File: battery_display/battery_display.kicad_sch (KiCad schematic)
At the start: 20 parts, among them J1 FH34SRJ-24S-0.5SH_99_, Q1 ZXM61N03F, Q2 ZXM61N03F, SW1 Button-THT - 2-1825910-7

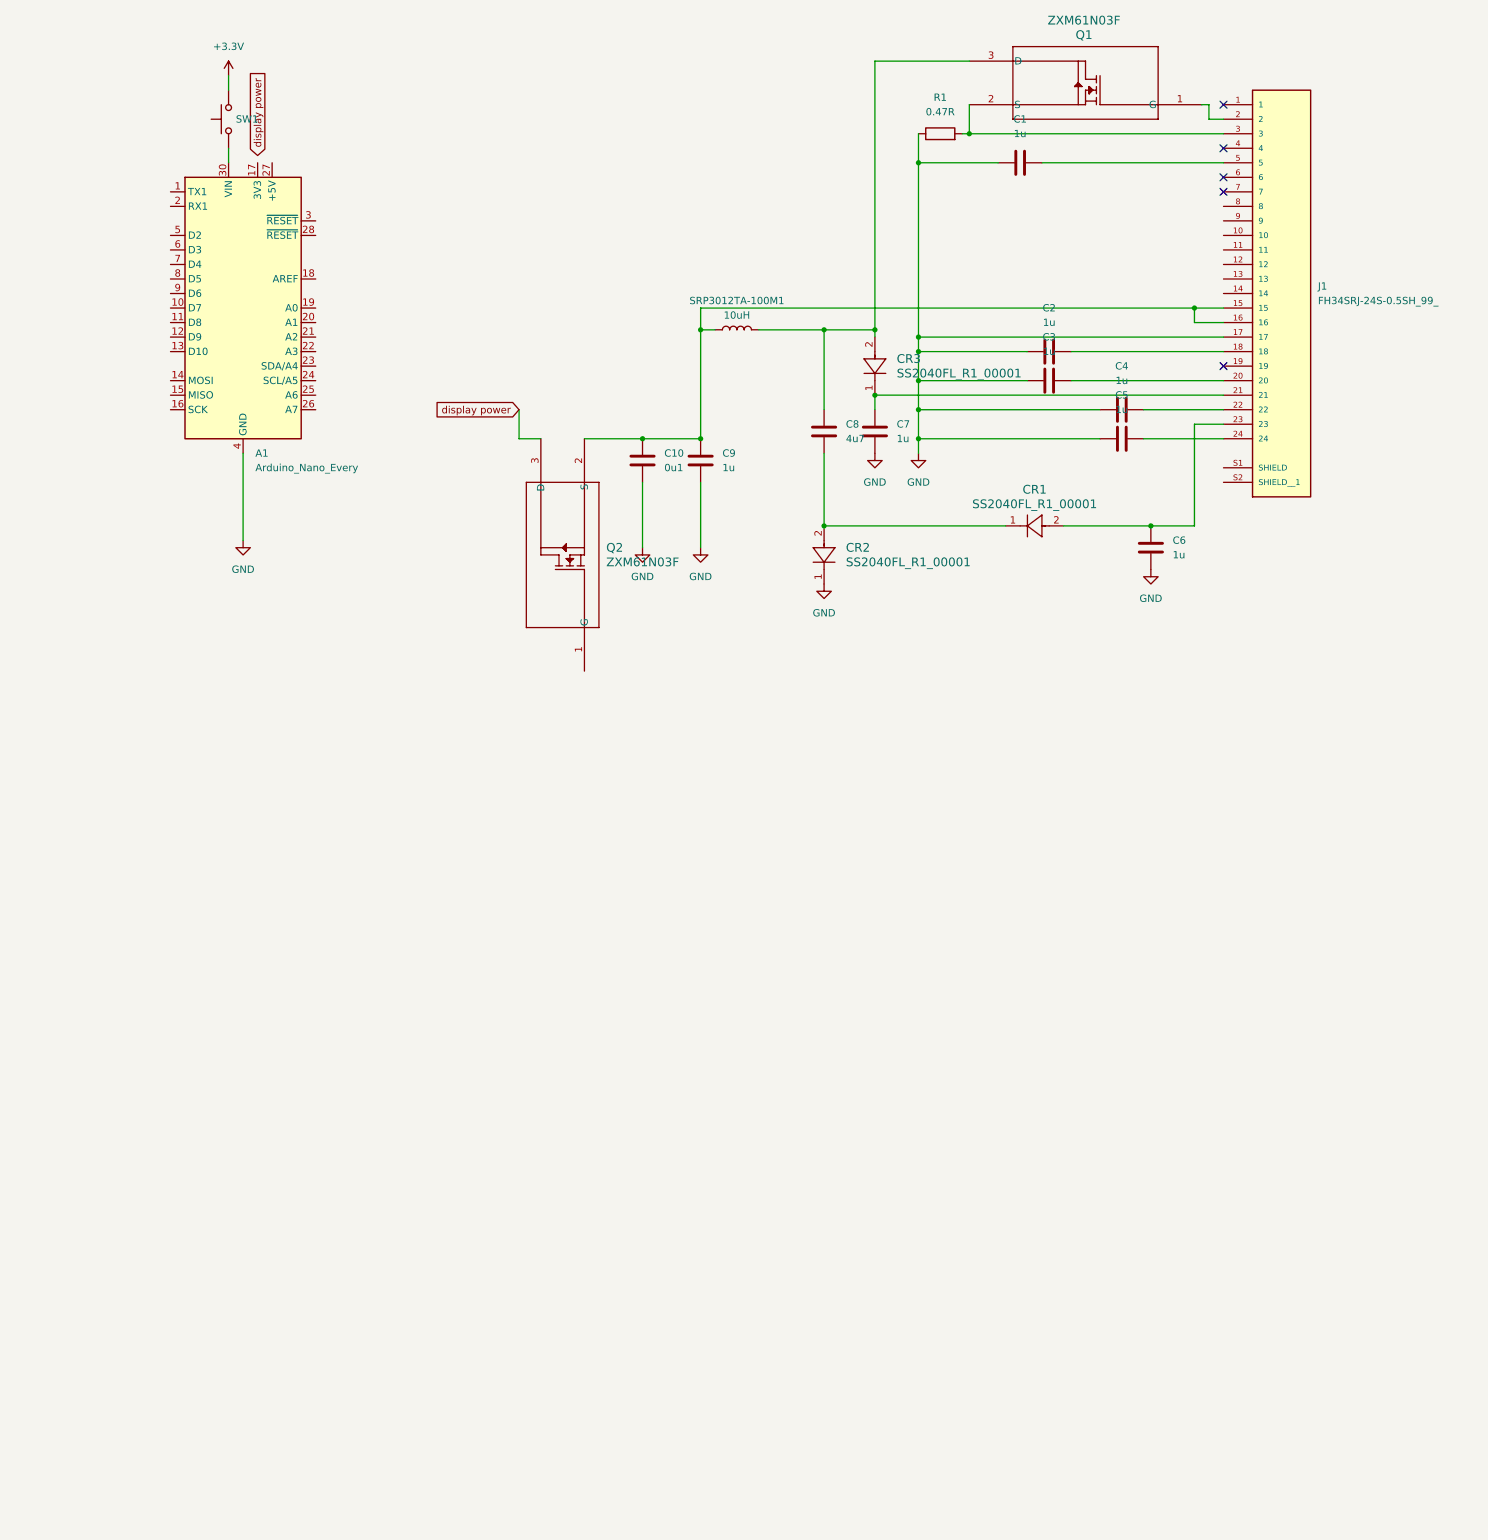
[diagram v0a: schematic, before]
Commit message: Completed PCB Layout
- also added voltage divider for reading voltage of the battery
- next step ask coco for conformation
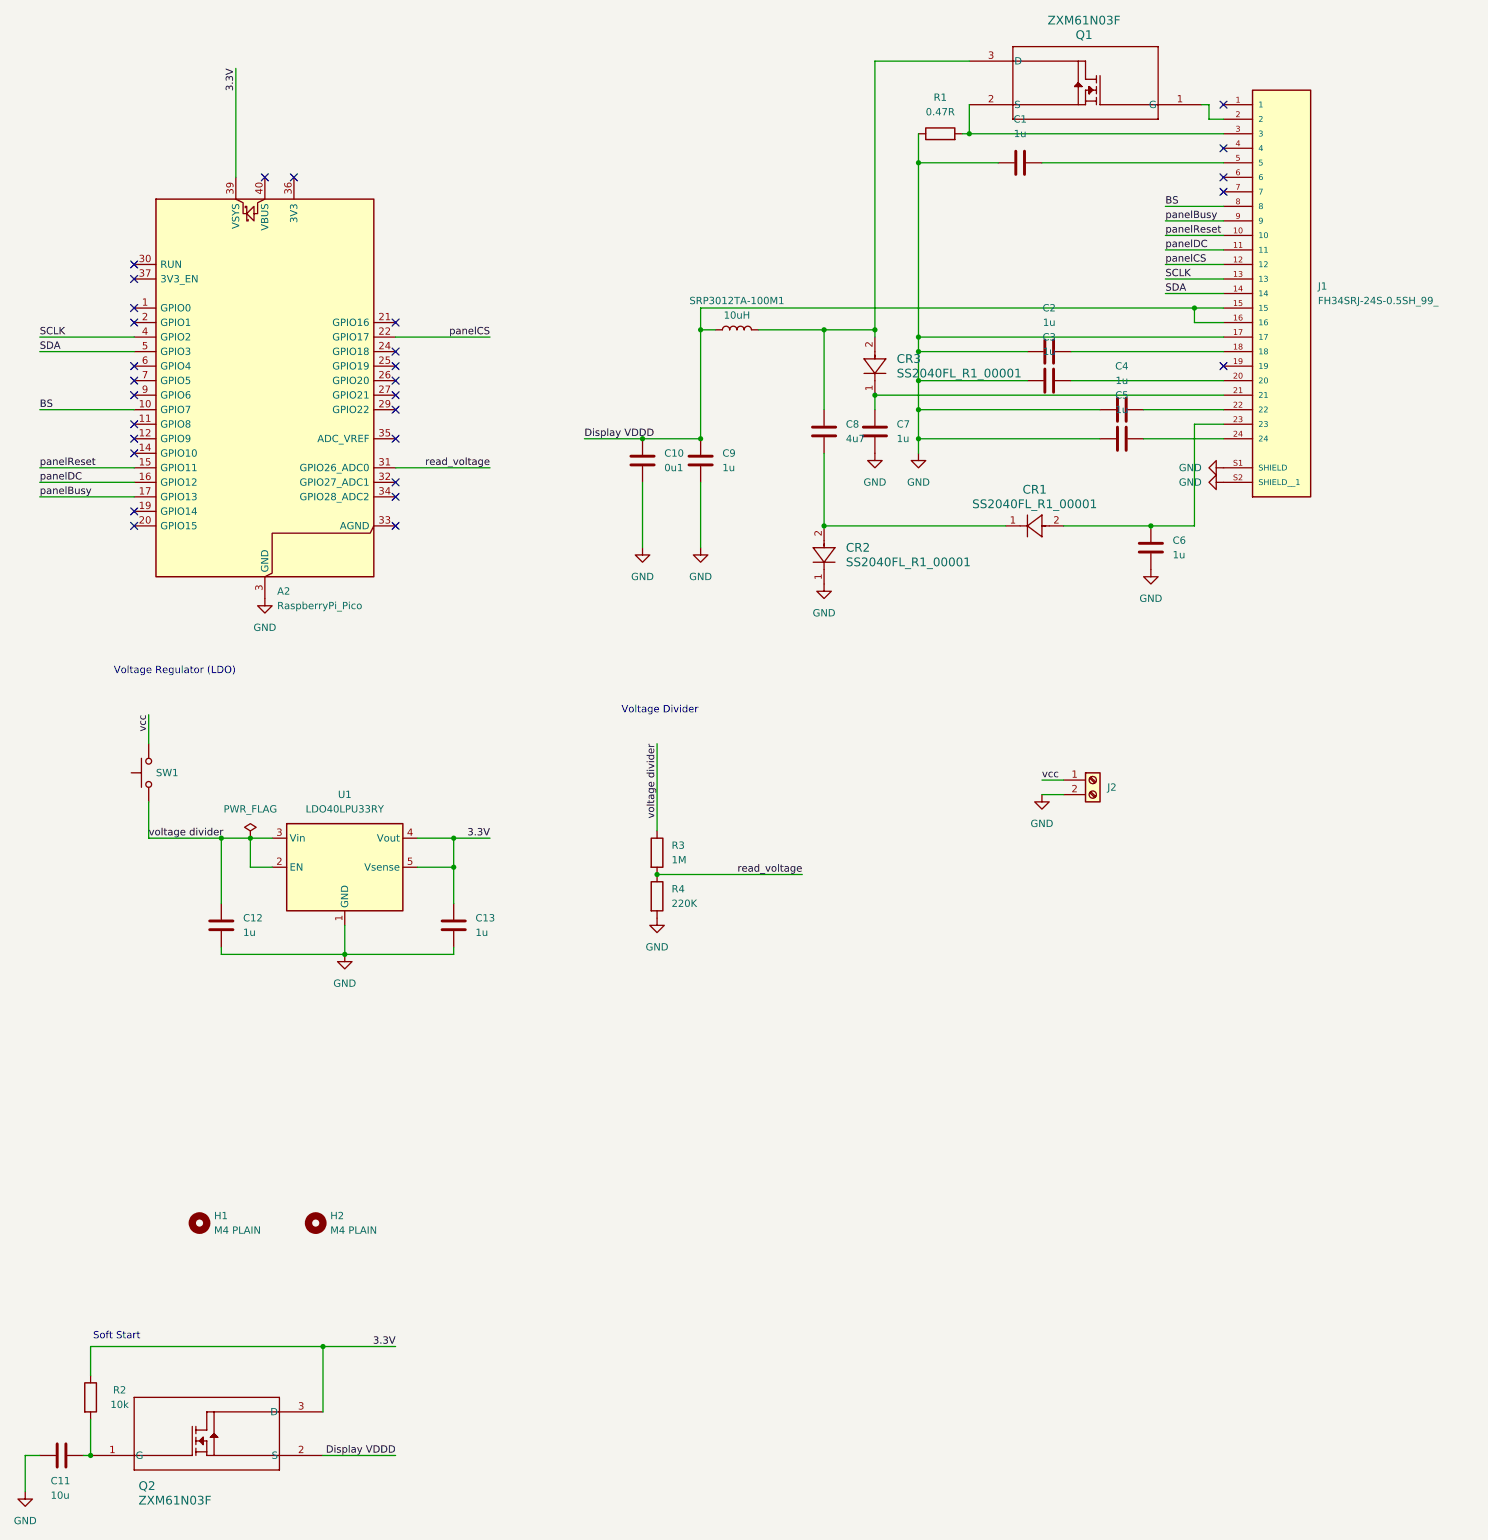
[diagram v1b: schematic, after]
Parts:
- removed A1: Arduino_Nano_Every, Module:Arduino_Nano, symbol MCU_Module:Arduino_Nano_Every
- added A2: RaspberryPi_Pico, Module:RaspberryPi_Pico_Common_Unspecified, symbol MCU_Module:RaspberryPi_Pico
- added C11: 10u, rsx_capacitors:C_0805_2012Metric, symbol rsx_Capacitors:10u
- added C12, C13: 1u, rsx_capacitors:C_0805_2012Metric, symbol rsx_Capacitors:1u
- added H1, H2: M4 PLAIN, rsx_misc:MountingHole_4.5mm, symbol rsx_misc:M4 PLAIN
- added J2: Screw_Terminal_2x2.54, rsx_headers_screw:Wurth_691210910002, symbol rsx_header_screw:Screw_Terminal_2x2.54
- added R2: 10k, rsx_resistors:R_0603_1608Metric, symbol rsx_Resistors:10k
- added R3: 1M, rsx_resistors:R_0603_1608Metric, symbol rsx_Resistors:1M
- added R4: 220K, rsx_resistors:R_0603_1608Metric, symbol rsx_Resistors:220K
- added U1: LDO40LPU33RY, Package_DFN_QFN:DFN-6-1EP_3x3mm_P0.95mm_EP1.7x2.6mm, symbol Regulator_Linear:LDO40LPU33RY
- J1: DPN (none) -> H124725CT-ND; MPN (none) -> FH34SRJ-24S-0.5SH(99)
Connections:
- net GND: now also J1.S1 (SHIELD), J1.S2 (SHIELD__1), A2.13 (GND), A2.18 (GND), A2.23 (GND), A2.28 (GND), A2.3 (GND), A2.38 (GND), A2.8 (GND), C11.2, C12.2, C13.2, J2.2 (Pin_2), R4.2, U1.1 (GND), U1.7 (GND)
- net panelReset: now reaches J1.10
- net panelReset: now also A2.15 (GPIO11)
- net panelDC: now reaches J1.11
- net panelDC: now also A2.16 (GPIO12)
- net panelCS: now reaches J1.12
- net panelCS: now also A2.22 (GPIO17)
- net SCLK: now reaches J1.13
- net SCLK: now also A2.4 (GPIO2)
- net SDA: now reaches J1.14
- net SDA: now also A2.5 (GPIO3)
- net Display VDDD: now reaches C10.1, C9.1, J1.15, J1.16, Q2.2 (S), SRP3012TA-100M1.1
- net BS: now reaches J1.8
- net BS: now also A2.10 (GPIO7)
- net panelBusy: now reaches J1.9
- net panelBusy: now also A2.17 (GPIO13)
- net voltage divider: now reaches SW1.1
- net voltage divider: now also C12.1, R3.1, U1.2 (EN), U1.3 (Vin)
- net at Q2.1 (G): now also C11.1, R2.2
- net +3.3V renamed vcc
- net vcc: now also J2.1 (Pin_1)
- net display power renamed 3.3V
- net 3.3V: now also A2.39 (VSYS), C13.1, R2.1, U1.4 (Vout), U1.5 (Vsense)
- new net read_voltage: A2.31 (GPIO26_ADC0), R3.2, R4.1
- no-connect marks 5 -> 29
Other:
- note added: "Soft Start"
- note added: "Voltage Divider"
- note added: "Voltage Regulator (LDO)"
- moved on the sheet: Q2, SW1

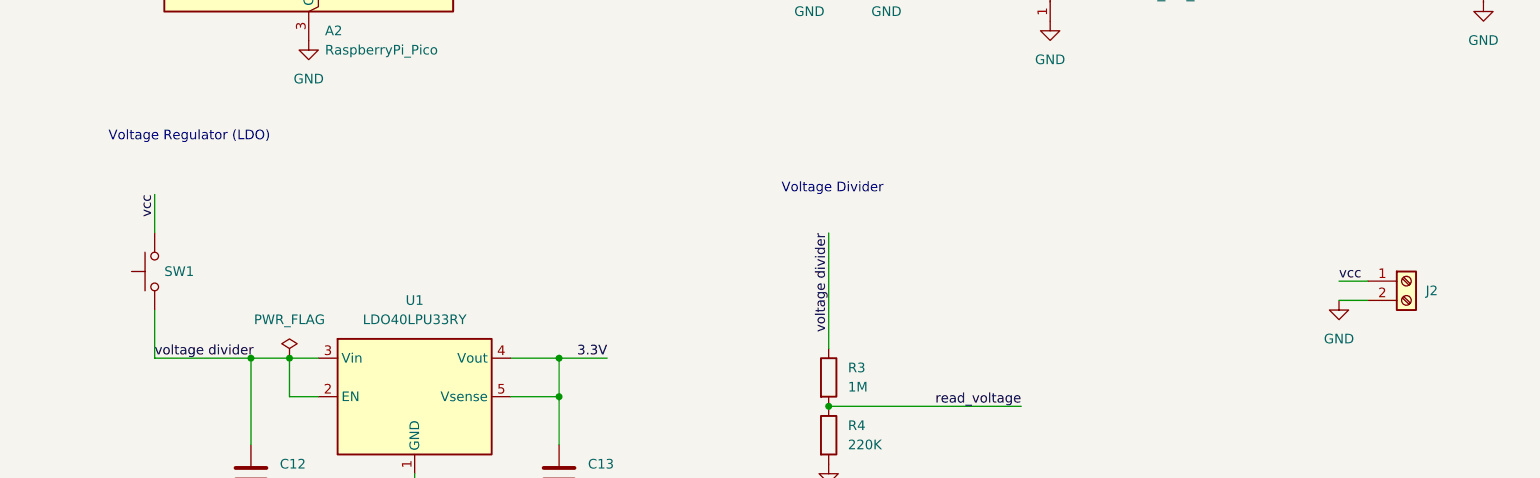
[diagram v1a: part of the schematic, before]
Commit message: Reapply "Added some small fixes"
This reverts commit d414565db0f35087673e5f9750bdaf74336bf2be.
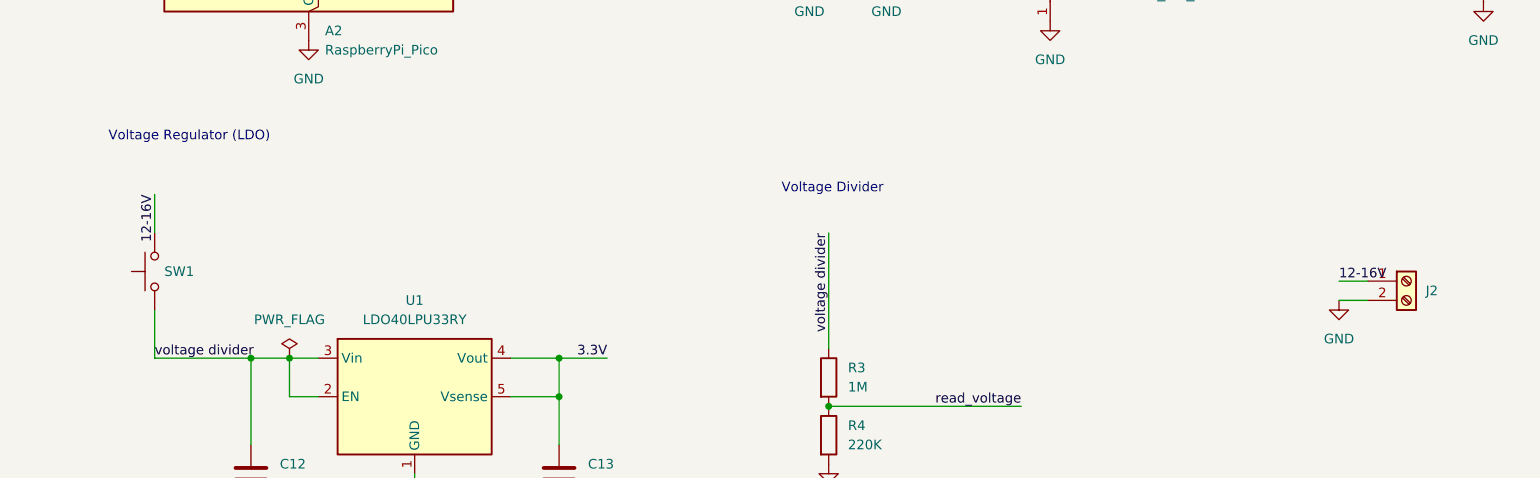
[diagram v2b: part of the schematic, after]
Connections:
- net vcc renamed 12-16V
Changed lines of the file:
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@@
 		)
 	)
-	(label "vcc"
+	(label "12-16V"
 		(at 39.37 139.7 270)
 		(effects
@@
 		)
 	)
-	(label "vcc"
+	(label "12-16V"
 		(at 195.58 151.13 0)
 		(effects

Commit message: Moved the display connector closer to the RPi
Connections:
- net SCLK: now also A2.27 (GPIO21); no longer A2.4 (GPIO2)
- net SDA: now also A2.26 (GPIO20); no longer A2.5 (GPIO3)
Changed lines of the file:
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@@
+	)
+	(no_connect
+		(at 36.83 76.2)
 	)
 	(no_connect
@@
 	)
 	(no_connect
-		(at 82.55 81.28)
+		(at 36.83 73.66)
 	)
 	(no_connect
@@
 	)
 	(no_connect
-		(at 82.55 83.82)
-	)
-	(no_connect
 		(at 64.77 45.72)
 	)
@@
 	(wire
 		(pts
+			(xy 82.55 83.82) (xy 99.06 83.82)
+		)
+		(stroke
+			(width 0)
+			(type default)
+		)
+	)
+	(wire
+		(pts
 			(xy 29.21 255.27) (xy 29.21 250.19)
 		)
@@
 	(wire
 		(pts
-			(xy 20.32 76.2) (xy 36.83 76.2)
-		)
-		(stroke
-			(width 0)
-			(type default)
-		)
-	)
-	(wire
-		(pts
-			(xy 20.32 73.66) (xy 36.83 73.66)
-		)
-		(stroke
-			(width 0)
-			(type default)
-		)
-	)
-	(wire
-		(pts
 			(xy 173.99 86.36) (xy 205.74 86.36)
 		)
@@
 		(pts
 			(xy 17.78 269.24) (xy 17.78 275.59)
+		)
+		(stroke
+			(width 0)
+			(type default)
+		)
+	)
+	(wire
+		(pts
+			(xy 82.55 81.28) (xy 99.06 81.28)
 		)
 		(stroke
@@
 		)
 	)
+	(label "SCLK"
+		(at 99.06 83.82 180)
+		(effects
+			(font
+				(size 1.27 1.27)
+			)
+			(justify right bottom)
+		)
+	)
 	(label "panelDC"
 		(at 20.32 99.06 0)
@@
 	)
 	(label "SDA"
-		(at 20.32 76.2 0)
-		(effects
-			(font
-				(size 1.27 1.27)
-			)
-			(justify left bottom)
-		)
-	)
-	(label "SDA"
 		(at 217.17 66.04 0)
 		(effects
@@
 		)
 	)
+	(label "SDA"
+		(at 99.06 81.28 180)
+		(effects
+			(font
+				(size 1.27 1.27)
+			)
+			(justify right bottom)
+		)
+	)
 	(label "read_voltage"
 		(at 99.06 96.52 180)
@@
 		(effects
 			(font
-				(size 1.27 1.27)
-			)
-			(justify left bottom)
-		)
-	)
-	(label "SCLK"
-		(at 20.32 73.66 0)
-		(effects
-			(font

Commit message: fixed traumatic errors
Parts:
- removed C10: 0u1, Capacitor_SMD:C_01005_0402Metric, symbol rsx_Capacitors:0u1_0402
- added C14: 100n, CAPC17595_95N_KEM, symbol rsx_Capacitors:100n
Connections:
- net Display VDDD: now also C14.2
- net GND: now also C14.1
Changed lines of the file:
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@@
 	)
 	(junction
+		(at 125.73 91.44)
+		(diameter 0)
+		(color 0 0 0 0)
+	)
+	(junction
 		(at 69.85 250.19)
 		(diameter 0)
@@
 	)
 	(junction
-		(at 125.73 91.44)
-		(diameter 0)
-		(color 0 0 0 0)
-	)
-	(junction
 		(at 173.99 73.66)
 		(diameter 0)
@@
 	(wire
 		(pts
-			(xy 125.73 91.44) (xy 135.89 91.44)
+			(xy 115.57 91.44) (xy 125.73 91.44)
 		)
 		(stroke
@@
 	(wire
 		(pts
-			(xy 173.99 76.2) (xy 193.04 76.2)
+			(xy 125.73 91.44) (xy 135.89 91.44)
 		)
 		(stroke
@@
 	(wire
 		(pts
-			(xy 115.57 91.44) (xy 125.73 91.44)
+			(xy 173.99 76.2) (xy 193.04 76.2)
 		)
 		(stroke
@@
 	)
 	(symbol
-		(lib_id "rsx_Capacitors:0u1_0402")
-		(at 125.73 95.25 0)
-		(unit 1)
-		(exclude_from_sim no)
-		(in_bom yes)
-		(on_board yes)
-		(dnp no)
-		(fields_autoplaced yes)
-		(property "Reference" "C10"
-			(at 129.54 93.9799 0)
-			(effects
-				(font
-					(size 1.27 1.27)
-				)
-				(justify left)
-			)
-		)
-		(property "Value" "0u1"
-			(at 129.54 96.5199 0)
-			(effects
-				(font
-					(size 1.27 1.27)
-				)
-				(justify left)
-			)
-		)
-		(property "Footprint" "Capacitor_SMD:C_01005_0402Metric"
-			(at 126.6952 99.06 0)
-			(effects
-				(font
-					(size 1.27 1.27)
-				)
-				(hide yes)
-			)
-		)
-		(property "Datasheet" "https://mm.digikey.com/Volume0/opasdata/d220001/medias/docus/503/CL05A104KA5NNNC.pdf"
-			(at 125.73 95.25 0)
-			(effects
-				(font
-					(size 1.27 1.27)
-				)
-				(hide yes)
-			)
-		)
-		(property "Description" "CAP CER 0.1UF 25V X5R 0402"
-			(at 125.73 95.25 0)
-			(effects
-				(font
-					(size 1.27 1.27)
-				)
-				(hide yes)
-			)
-		)
-		(property "MFR" "Samsung Electro-Mechanics"
-			(at 125.73 95.25 0)
-			(effects
-				(font
-					(size 1.27 1.27)
-				)
-				(hide yes)
-			)
-		)
-		(property "DPN" "1276-1043-1-ND"
-			(at 125.73 95.25 0)
-			(effects
-				(font
-					(size 1.27 1.27)
-				)
-				(hide yes)
-			)
-		)
-		(property "MPN" "CL05A104KA5NNNC"
-			(at 125.73 95.25 0)
-			(effects
-				(font
-					(size 1.27 1.27)
-				)
-				(hide yes)
-			)
-		)
-		(pin "1"
-		)
-		(pin "2"
-		)
-		(instances
-			(project ""
-				(path "/9c37534e-0246-46b3-81ad-6273e0189fcc"
-					(reference "C10")
-					(unit 1)
-				)
-			)
-		)
-	)
-	(symbol
 		(lib_id "power:GND")
 		(at 227.33 96.52 270)
@@
 					(unit 1)
 				)
+			)
+		)
+	)
+	(symbol
+		(lib_id "rsx_Capacitors:100n")
+		(at 125.73 99.06 90)
+		(unit 1)
+		(exclude_from_sim no)
+		(in_bom yes)
+		(on_board yes)
+		(dnp no)
+		(fields_autoplaced yes)
+		(property "Reference" "C14"
+			(at 129.54 93.9799 90)
+			(effects
+				(font
+					(size 1.524 1.524)
+				)
+				(justify right)
+			)
+		)
+		(property "Value" "100n"
+			(at 129.54 96.5199 90)
+			(effects
+				(font
+					(size 1.524 1.524)
+				)
+				(justify right)
+			)
+		)
+		(property "Footprint" "CAPC17595_95N_KEM"
+			(at 125.73 99.06 0)
+			(effects
+				(font
+					(size 1.27 1.27)
+					(italic yes)
+				)
+				(hide yes)
+			)
+		)
+		(property "Datasheet" "https://content.kemet.com/datasheets/KEM_C1002_X7R_SMD.pdf"
+			(at 125.73 99.06 0)
+			(effects
+				(font
+					(size 1.27 1.27)
+					(italic yes)
+				)
+				(hide yes)
+			)
+		)
+		(property "Description" "0.1 µF ±10% 50V Ceramic Capacitor X7R 0603 (1608 Metric)"
+			(at 125.73 99.06 0)
+			(effects
+				(font
+					(size 1.27 1.27)
+				)
+				(hide yes)
+			)
+		)
+		(property "DPN" "399-C0603C104K5RACTUCT-ND"
+			(at 125.73 99.06 0)
+			(effects
+				(font
+					(size 1.27 1.27)
+				)
+				(hide yes)
+			)
+		)
+		(property "MPN" "C0603C104K5RACTU"
+			(at 125.73 99.06 0)
+			(effects
+				(font
+					(size 1.27 1.27)
+				)
+				(hide yes)
+			)
+		)
+		(pin "2"
+		)
+		(pin "1"
+		)
+		(instances
+			(project ""
+				(path "/9c37534e-0246-46b3-81ad-6273e0189fcc"
+					(reference "C14")
+					(unit 1)
+				)
